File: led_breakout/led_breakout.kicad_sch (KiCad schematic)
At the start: 19 parts, among them J1 S-, J2 P, J3 P, J4 S+

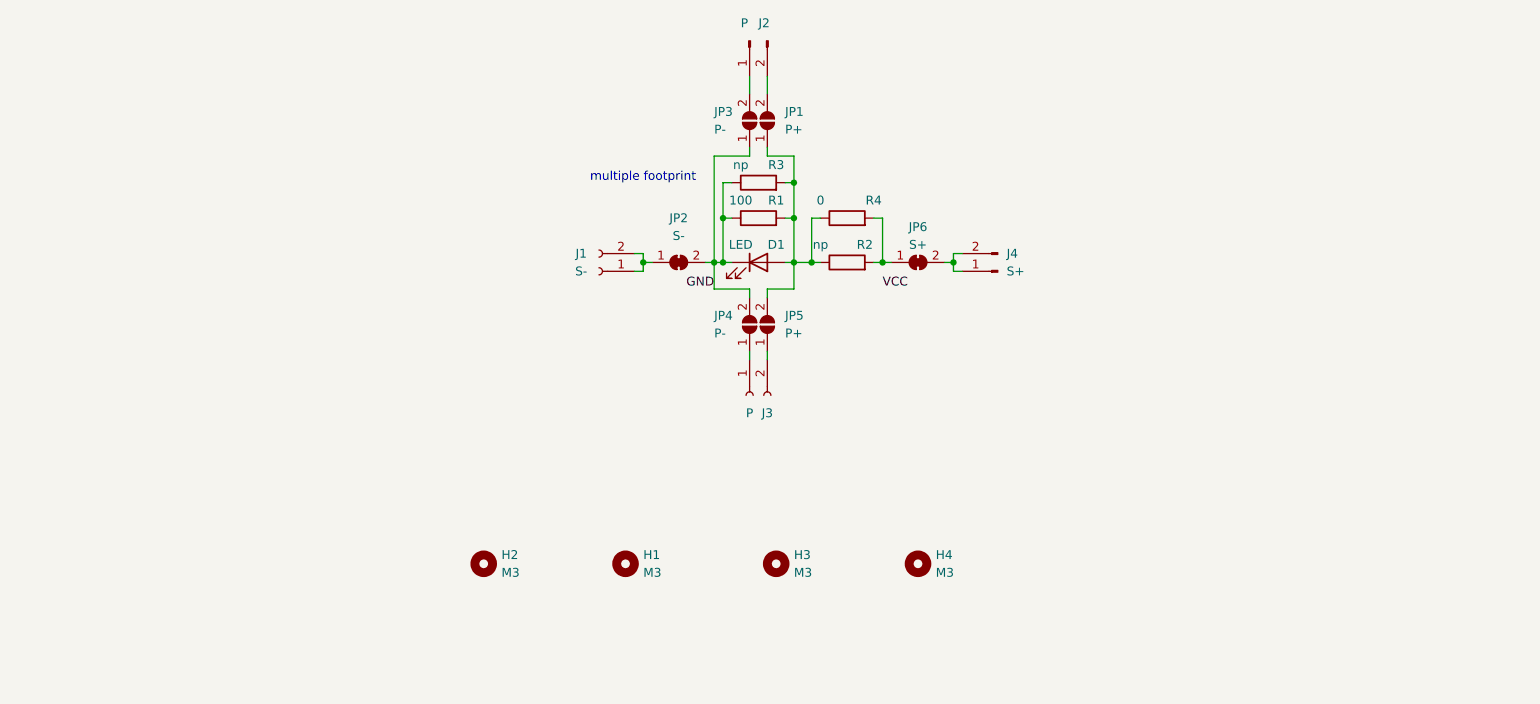
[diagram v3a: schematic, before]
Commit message: Add references for external components
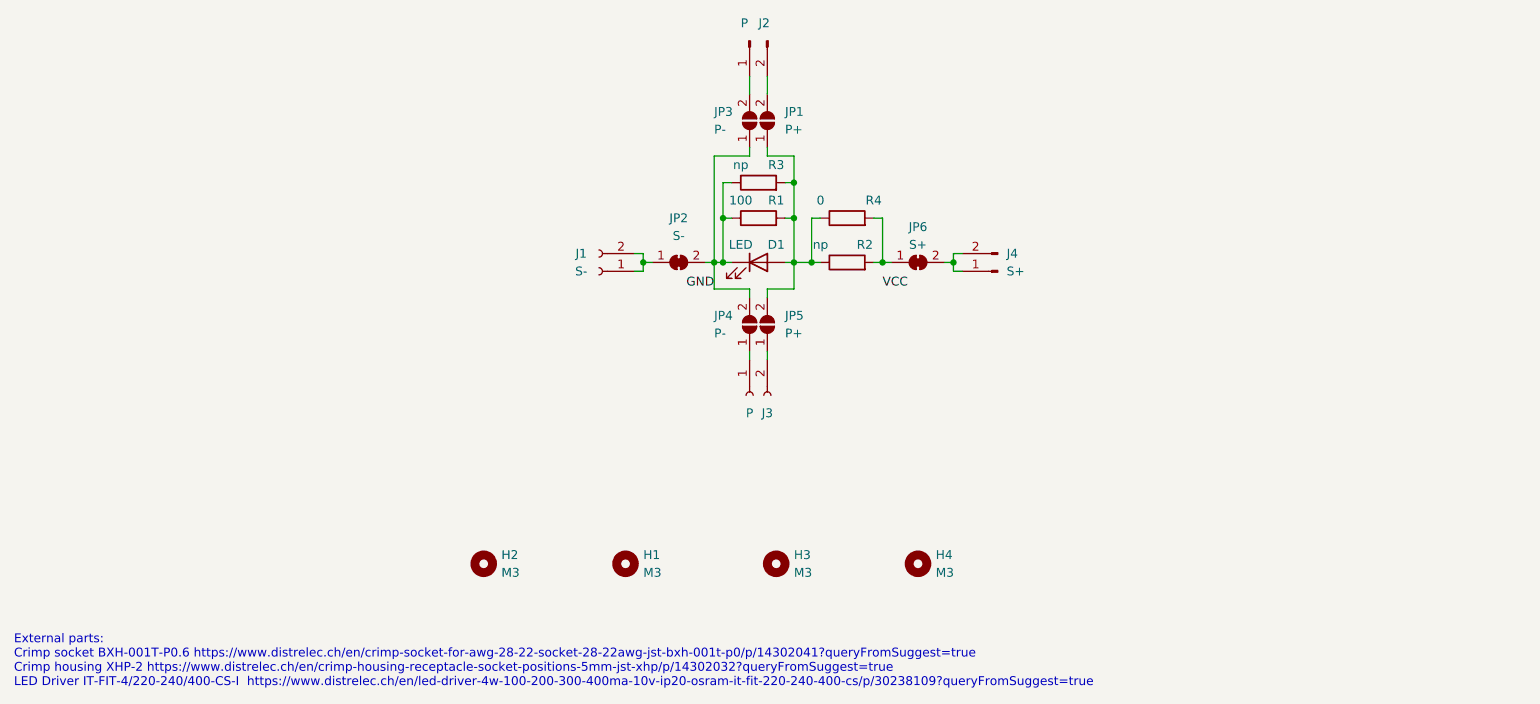
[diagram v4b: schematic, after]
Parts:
- J3: Alternative for single light  (none) -> https://www.digikey.ch/fr/products/detail/jst-sales-america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
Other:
- note added: "External parts: Crimp socket BXH-001T-P0.6 https://www.distrelec.ch/en/crimp-socket-for-awg-28-22-socket-28-22awg-jst-bxh-001t-p0/p/14302041?queryFromSuggest=true Crimp housing XHP-2 https://www.distrelec.ch/en/crimp-housing-receptacle-socket-positions-5mm-jst-xhp/p/14302032?queryFromSuggest=true LED Driver IT-FIT-4/220-240/400-CS-I https://www.distrelec.ch/en/led-driver-4w-100-200-300-400ma-10v-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"
- note removed: "multiple footprint"
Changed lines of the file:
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@@
     (stroke (width 0) (type default) (color 0 0 0 0))
   )
-  (text "multiple footprint" (at 139.7 83.82 0)
+  (text "External parts:\nCrimp socket BXH-001T-P0.6 https://www.distrelec.ch/en/crimp-socket-for-awg-28-22-socket-28-22awg-jst-bxh-001t-p0/p/14302041?queryFromSuggest=true\nCrimp housing XHP-2 https://www.distrelec.ch/en/crimp-housing-receptacle-socket-positions-5mm-jst-xhp/p/14302032?queryFromSuggest=true\nLED Driver IT-FIT-4/220-240/400-CS-I  https://www.distrelec.ch/en/led-driver-4w-100-200-300-400ma-10v-ip20-osram-it-fit-220-240-400-cs/p/30238109?queryFromSuggest=true"
+    (at 57.15 156.21 0)
     (effects (font (size 1.27 1.27)) (justify left bottom))
   )
@@
       (effects (font (size 1.27 1.27)) hide)
     )
+    (property "Alternative for single light " "https://www.digikey.ch/fr/products/detail/jst-sales-america-inc/S2B-XH-A-1-LF-SN/9961922?s=N4IgTCBcDaICwFYEFo5jANmQOwCYgF0BfIA" (id 7) (at 162.56 114.3 90)
+      (effects (font (size 1.27 1.27)) hide)
+    )
